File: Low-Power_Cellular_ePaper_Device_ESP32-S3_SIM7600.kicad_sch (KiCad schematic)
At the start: 100 parts, among them J1 USB-C, J2 BATT (JST-PH), J3 nanoSIM_GCT_SIM8060, J4 MAIN_ANT_UFL, J5 GNSS_ANT_UFL, J6 FH12-24S-0.5SH, J7 Qwiic / STEMMA QT, Q1 AO3401A, Q10 BSS138, Q2 BSS138, Q3 BSS138, Q4 BSS138, Q6 AO3401A, Q7 BSS138, Q8 AO3401A, Q9 BSS138, SW1 RESET, SW2 BOOT, U1 ESP32-S3-WROOM-1, U2 SIMCom_SIM7600G, U3 TXS0104ED, U4 MCP73831-2-OT, U5 RT9080-33 / AP2112K, U6 SHT40-AD1B

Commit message: Repair CAD metadata and document blocking electrical review findings
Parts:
- C31, C32: now not fitted
- U2: symbol SIMCom_SIM7600G -> Cellular:SIMCom_SIM7600G
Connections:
- new net: J1.A1 (GND), J1.A12 (GND), J1.B1 (GND), J1.B12 (GND)
- new net: J1.A4 (VBUS), J1.A9 (VBUS), J1.B4 (VBUS), J1.B9 (VBUS)
- new net: U1.1 (GND), U1.40 (GND), U1.41 (GND)

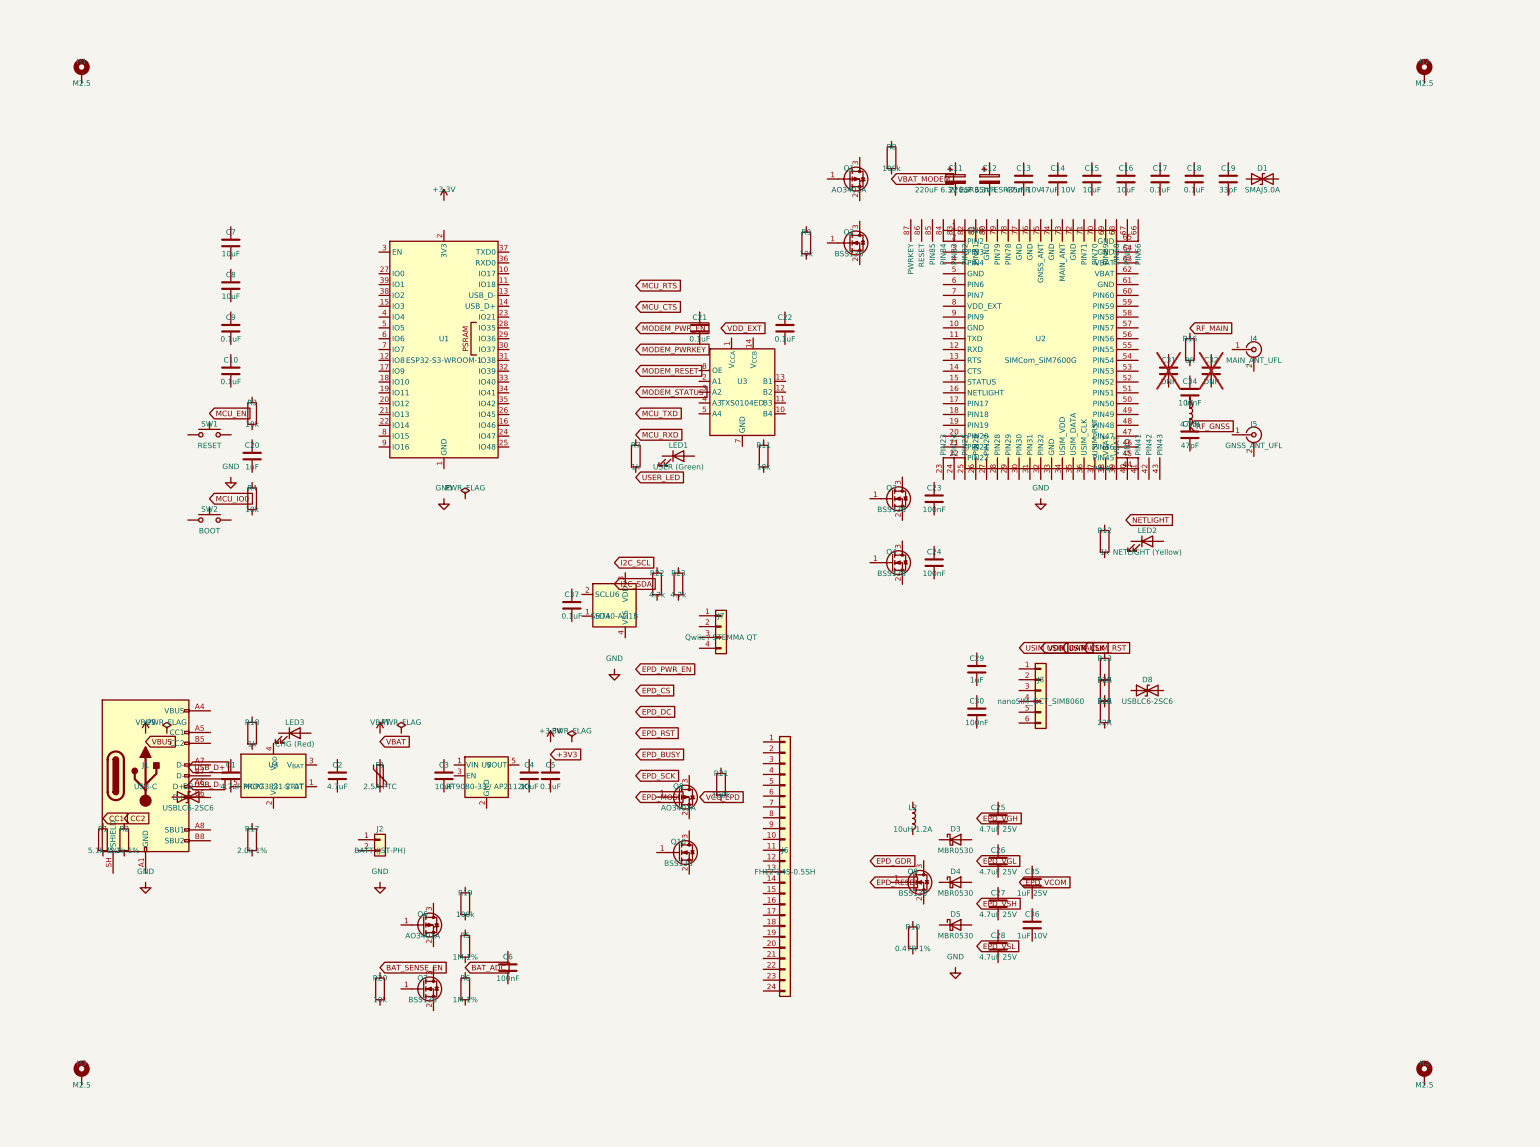
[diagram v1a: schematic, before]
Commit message: Redesign cellular ePaper revision B and close native CAD connectivity checks
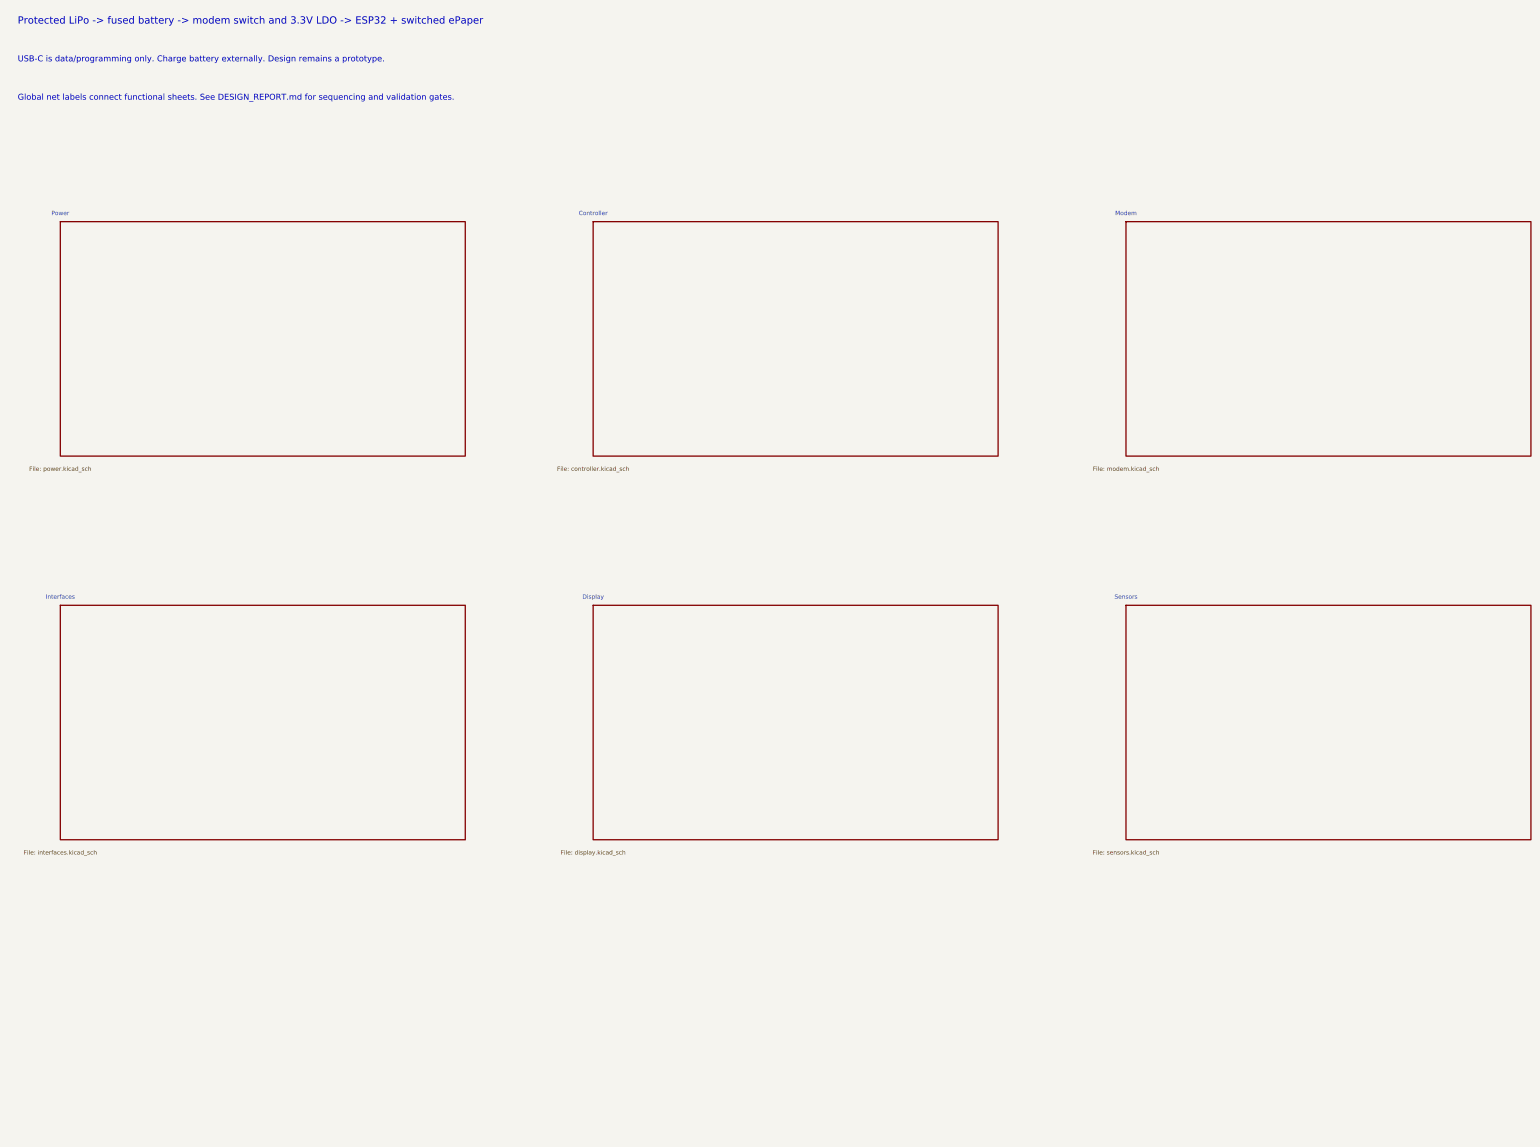
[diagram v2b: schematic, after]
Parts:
- removed C1, C2: 4.7uF, Capacitor_SMD:C_0805_2012Metric, symbol Device:C
- removed C10, C17, C18, C21, C22, C37, C5, C9: 0.1uF, Capacitor_SMD:C_0402_1005Metric, symbol Device:C
- removed C11, C12: 220uF 6.3V ESR35mR, Capacitor_Tantalum_SMD:CP_EIA-7343-31_Kemet-D, symbol Device:C_Polarized
- removed C13, C14: 47uF 10V, Capacitor_SMD:C_0805_2012Metric, symbol Device:C
- removed C15, C16: 10uF, Capacitor_SMD:C_0603_1608Metric, symbol Device:C
- removed C19: 33pF, Capacitor_SMD:C_0402_1005Metric, symbol Device:C
- removed C20, C29: 1uF, Capacitor_SMD:C_0603_1608Metric, symbol Device:C
- removed C23, C24, C30, C34, C6: 100nF, Capacitor_SMD:C_0402_1005Metric, symbol Device:C
- removed C25, C26, C27, C28: 4.7uF 25V, Capacitor_SMD:C_0805_2012Metric, symbol Device:C
- removed C3, C4, C7, C8: 10uF, Capacitor_SMD:C_0805_2012Metric, symbol Device:C
- removed C31, C32: DNP, Capacitor_SMD:C_0402_1005Metric, symbol Device:C
- removed C33: 47pF, Capacitor_SMD:C_0402_1005Metric, symbol Device:C
- removed C35: 1uF 25V, Capacitor_SMD:C_0805_2012Metric, symbol Device:C
- removed C36: 1uF 10V, Capacitor_SMD:C_0603_1608Metric, symbol Device:C
- removed D1: SMAJ5.0A, Diode_SMD:D_SMA, symbol Device:D_TVS
- removed D2, D8: USBLC6-2SC6, Package_TO_SOT_SMD:SOT-23-6, symbol Device:D_TVS
- removed D3, D4, D5: MBR0530, Diode_SMD:D_SOD-123, symbol Device:D_Schottky
- removed F1: 2.5A PTC, Fuse:Fuse_1206_3216Metric, symbol Device:Polyfuse
- removed H1, H2, H3, H4: M2.5, MountingHole:MountingHole_2.7mm_M2.5_Pad_Via, symbol Mechanical:MountingHole_Pad
- removed J1: USB-C, Connector_USB:USB_C_Receptacle_GCT_USB4085, symbol Connector:USB_C_Receptacle_USB2.0_16P
- removed J2: BATT (JST-PH), Connector_JST:JST_PH_S2B-PH-K_1x02_P2.00mm_Horizontal, symbol Connector_Generic:Conn_01x02
- removed J3: nanoSIM_GCT_SIM8060, Connector_Card:nanoSIM_GCT_SIM8060-6-0-14-00, symbol Connector_Generic:Conn_01x06
- removed J4: MAIN_ANT_UFL, Connector_Coaxial:U.FL_Hirose_U.FL-R-SMT-1_Vertical, symbol Connector:Conn_Coaxial
- removed J5: GNSS_ANT_UFL, Connector_Coaxial:U.FL_Hirose_U.FL-R-SMT-1_Vertical, symbol Connector:Conn_Coaxial
- removed J6: FH12-24S-0.5SH, Connector_FFC-FPC:Hirose_FH12-24S-0.5SH_1x24-1MP_P0.50mm_Horizontal, symbol Connector_Generic:Conn_01x24
- removed J7: Qwiic / STEMMA QT, Connector_JST:JST_SH_SM04B-SRSS-TB_1x04-1MP_P1.00mm_Horizontal, symbol Connector_Generic:Conn_01x04
- removed L1: 47nH, Inductor_SMD:L_0402_1005Metric, symbol Device:L
- removed L2: 10uH 1.2A, Inductor_SMD:L_1210_3225Metric, symbol Device:L
- removed LED1: USER (Green), LED_SMD:LED_0603_1608Metric, symbol Device:LED
- removed LED2: NETLIGHT (Yellow), LED_SMD:LED_0603_1608Metric, symbol Device:LED
- removed LED3: CHG (Red), LED_SMD:LED_0603_1608Metric, symbol Device:LED
- removed Q1, Q6, Q8: AO3401A, Package_TO_SOT_SMD:SOT-23, symbol Transistor_FET:AO3401A
- removed Q10, Q2, Q3, Q4, Q7, Q9: BSS138, Package_TO_SOT_SMD:SOT-23, symbol Transistor_FET:BSS138
- removed R1, R2: 5.1k 1%, Resistor_SMD:R_0603_1608Metric, symbol Device:R
- removed R10: 0.47R 1%, Resistor_SMD:R_0805_2012Metric, symbol Device:R
- removed R11, R20, R3, R4, R9: 10k, Resistor_SMD:R_0603_1608Metric, symbol Device:R
- removed R12, R18, R7: 1k, Resistor_SMD:R_0603_1608Metric, symbol Device:R
- removed R13, R14, R15: 22R, Resistor_SMD:R_0402_1005Metric, symbol Device:R
- removed R16: 0R, Resistor_SMD:R_0402_1005Metric, symbol Device:R
- removed R17: 2.0k 1%, Resistor_SMD:R_0603_1608Metric, symbol Device:R
- removed R19, R21, R8: 100k, Resistor_SMD:R_0603_1608Metric, symbol Device:R
- removed R22, R23: 4.7k, Resistor_SMD:R_0603_1608Metric, symbol Device:R
- removed R5, R6: 1M 1%, Resistor_SMD:R_0603_1608Metric, symbol Device:R
- removed SW1: RESET, Button_Switch_SMD:SW_Push_SPST_NO_Alps_SKRK, symbol Switch:SW_Push
- removed SW2: BOOT, Button_Switch_SMD:SW_Push_SPST_NO_Alps_SKRK, symbol Switch:SW_Push
- removed U1: ESP32-S3-WROOM-1, RF_Module:ESP32-S3-WROOM-1, symbol RF_Module:ESP32-S3-WROOM-1
- removed U2: SIMCom_SIM7600G, Low-Power_Cellular_ePaper_Device_ESP32-S3_SIM7600:SIMCom_SIM7600G, symbol Cellular:SIMCom_SIM7600G
- removed U3: TXS0104ED, Package_SO:SOIC-14_3.9x8.7mm_P1.27mm, symbol Logic_LevelTranslator:TXS0104ED
- removed U4: MCP73831-2-OT, Package_TO_SOT_SMD:SOT-23-5, symbol Battery_Management:MCP73831-2-OT
- removed U5: RT9080-33 / AP2112K, Package_TO_SOT_SMD:SOT-23-5, symbol Regulator_Linear:AP2112K-3.3
- removed U6: SHT40-AD1B, Sensor_Humidity:Sensirion_DFN-4_1.5x1.5mm_P0.8mm_SHT4x_NoCentralPad, symbol Sensor_Humidity:SHT4x
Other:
- added sheet Controller (controller.kicad_sch)
- added sheet Display (display.kicad_sch)
- added sheet Interfaces (interfaces.kicad_sch)
- added sheet Modem (modem.kicad_sch)
- added sheet Power (power.kicad_sch)
- added sheet Sensors (sensors.kicad_sch)
- note added: "Global net labels connect functional sheets. See DESIGN_REPORT.md for sequencing and validation gates."
- note added: "Protected LiPo -> fused battery -> modem switch and 3.3V LDO -> ESP32 + switched ePaper"
- note added: "USB-C is data/programming only. Charge battery externally. Design remains a prototype."
- company: IoT Hardware Engineering Portfolio -> Hector / xmyoot
- title: Low-Power Cellular e-Paper Device (ESP32-S3 + SIM7600) -> Cellular ePaper - revision B architecture
